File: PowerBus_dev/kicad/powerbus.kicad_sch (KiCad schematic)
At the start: 1 part, among them Q1 XT60_YELLOW

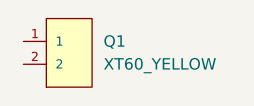
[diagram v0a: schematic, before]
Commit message: added symbols and footprints for xt90
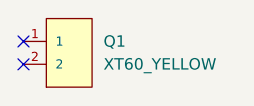
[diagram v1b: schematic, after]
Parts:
- Q1: footprint XT60_YELLOW:AMASS_XT60PB-M -> powerbus lib:AMASS_XT60PB-M
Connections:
- no-connect marks 0 -> 2
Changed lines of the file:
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@@
 	(generator_version "9.0")
 	(paper "A4")
+	(no_connect
+		(at 123.19 100.33)
+	)
+	(no_connect
+		(at 123.19 97.79)
+	)
 	(symbol
 		(lib_id "powerbus lib:XT60_YELLOW")
@@
 			)
 		)
-		(property "Footprint" "XT60_YELLOW:AMASS_XT60PB-M"
+		(property "Footprint" "powerbus lib:AMASS_XT60PB-M"
 			(at 128.27 97.79 0)
 			(effects
